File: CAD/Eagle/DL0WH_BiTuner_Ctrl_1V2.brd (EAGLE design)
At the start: 96.5 x 73 mm, 157 parts, among them Q0321 ABS07-32.768KHZ, U0101 STM32L476RXT_64PIN_LDO, U0601 MC33996, U0701 MC33996, U0801 MC33996, U0921 TS5A23166, U0941 LM2611, U0951 OPA354, U0961 OPA354, U0962 MCP4661-103E-MS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

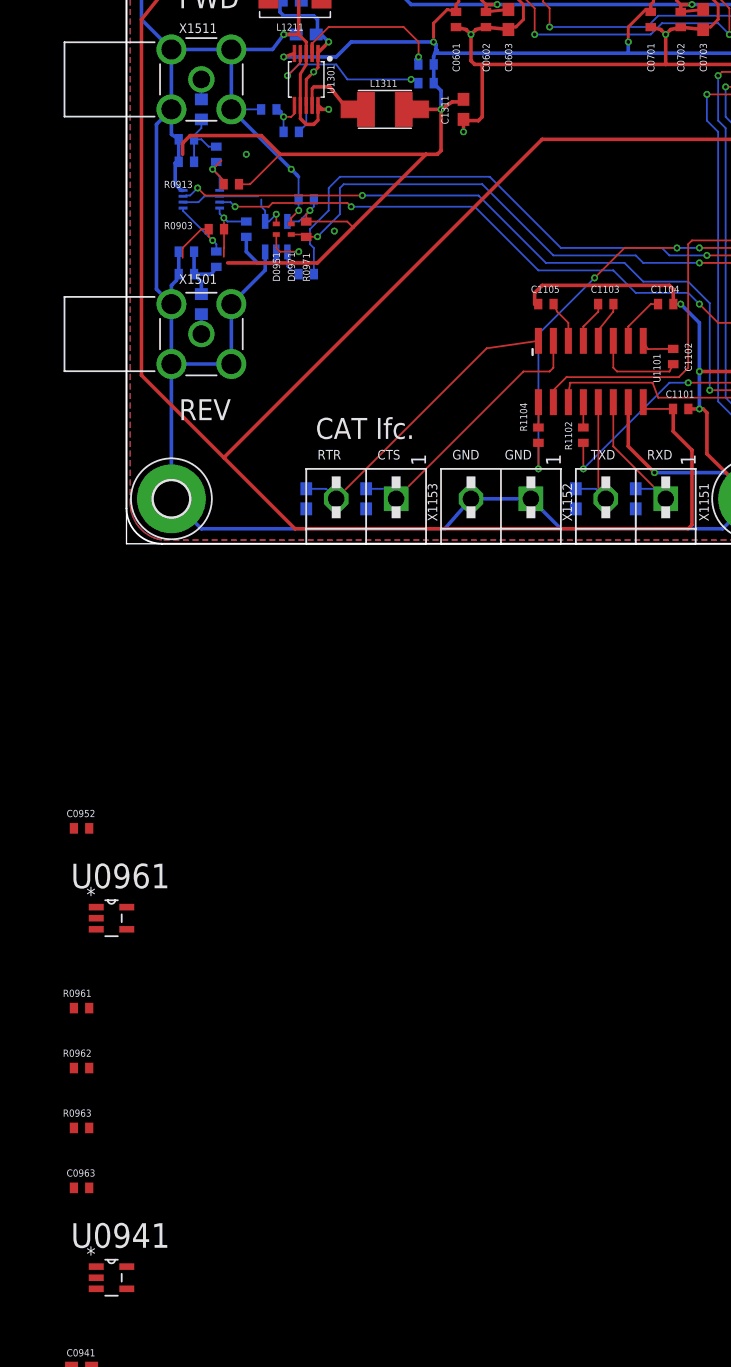
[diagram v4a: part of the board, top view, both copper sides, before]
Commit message: HW_1V2 - CAD/Eagle/lbr - df4iah_opamp package SOT-23-5 and SOT-23-6 text size fixed
Signed-off-by: Ulrich Habel <espero7757@gmx.net>
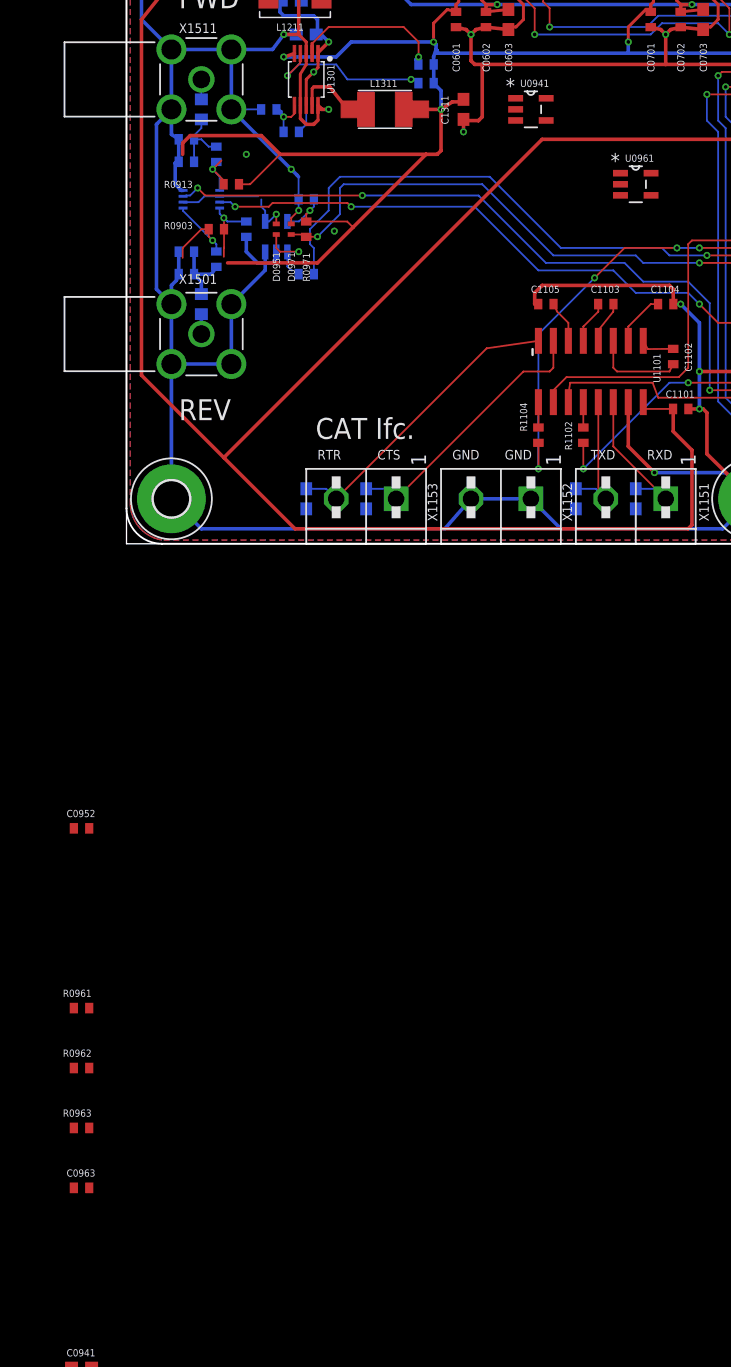
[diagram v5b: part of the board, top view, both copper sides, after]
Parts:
- moved U0941 105.2 mm to (34.3, 36.8)
- moved U0961 76.5 mm to (43.2, 30.5)
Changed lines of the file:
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@@
 <element name="D1221" library="df4iah_diode" package="SOD80C" value="CRS08" x="83.82" y="29.21" rot="R270"/>
 <element name="C0952" library="df4iah_rcl" package="C0402" value="100nF" x="-3.81" y="-24.13"/>
-<element name="U0961" library="df4iah_opamp" package="SOT-23-5" value="OPA354" x="-1.27" y="-31.75">
-<attribute name="OC_NEWARK" value="-" x="-1.27" y="-31.75" size="0.6096" layer="27" ratio="10" display="off"/>
-<attribute name="SUPPLIER" value="Texas Instruments" x="-1.27" y="-31.75" size="0.6096" layer="27" ratio="10" display="off"/>
-<attribute name="PACKAGE" value="SOT-23-5" x="-1.27" y="-31.75" size="0.6096" layer="27" ratio="10" display="off"/>
-<attribute name="MPN" value="OPA354AIDBVT" x="-1.27" y="-31.75" size="0.6096" layer="27" ratio="10" display="off"/>
-<attribute name="OC_FARNELL" value="1207050" x="-1.27" y="-31.75" size="0.6096" layer="27" ratio="10" display="off"/>
+<element name="U0961" library="df4iah_opamp" package="SOT-23-5" value="OPA354" x="43.18" y="30.48">
+<attribute name="OC_NEWARK" value="-" x="43.18" y="30.48" size="0.6096" layer="27" ratio="10" display="off"/>
+<attribute name="SUPPLIER" value="Texas Instruments" x="43.18" y="30.48" size="0.6096" layer="27" ratio="10" display="off"/>
+<attribute name="PACKAGE" value="SOT-23-5" x="43.18" y="30.48" size="0.6096" layer="27" ratio="10" display="off"/>
+<attribute name="MPN" value="OPA354AIDBVT" x="43.18" y="30.48" size="0.6096" layer="27" ratio="10" display="off"/>
+<attribute name="OC_FARNELL" value="1207050" x="43.18" y="30.48" size="0.6096" layer="27" ratio="10" display="off"/>
 </element>
 <element name="R0961" library="df4iah_rcl" package="R0402" value="1kR" x="-3.81" y="-39.37"/>
@@
 <element name="R0963" library="df4iah_rcl" package="R0402" value="10kR" x="-3.81" y="-49.53"/>
 <element name="C0963" library="df4iah_rcl" package="C0402" value="100pF" x="-3.81" y="-54.61"/>
-<element name="U0941" library="df4iah_powersupply" package="SOT95P280X145-5N" value="LM2611" x="-1.27" y="-62.23"/>
+<element name="U0941" library="df4iah_powersupply" package="SOT95P280X145-5N" value="LM2611" x="34.29" y="36.83"/>
 <element name="C0941" library="df4iah_rcl" package="C0603" value="22uF" x="-3.81" y="-69.85"/>
 <element name="L0941" library="df4iah_rcl" package="L1812" value="20uH" x="-2.54" y="-76.2"/>
@@
 <wire x1="-9.32" y1="-90.17" x2="-8.04" y2="-95.25" width="0" layer="19" extent="1-1"/>
 <wire x1="-2.96" y1="-69.85" x2="-9.32" y2="-90.17" width="0" layer="19" extent="1-1"/>
-<wire x1="-2.5654" y1="-62.23" x2="-2.96" y2="-69.85" width="0" layer="19" extent="1-1"/>
-<wire x1="-2.5654" y1="-32.6898" x2="-2.5654" y2="-62.23" width="0" layer="19" extent="1-1"/>
-<wire x1="-3.16" y1="-24.13" x2="-2.5654" y2="-32.6898" width="0" layer="19" extent="1-1"/>
+<wire x1="32.9946" y1="36.83" x2="-2.96" y2="-69.85" width="0" layer="19" extent="1-1"/>
+<wire x1="41.8846" y1="29.5402" x2="32.9946" y2="36.83" width="0" layer="19" extent="1-1"/>
+<wire x1="-3.16" y1="-24.13" x2="41.8846" y2="29.5402" width="0" layer="19" extent="1-1"/>
 <wire x1="6.35" y1="1.27" x2="-3.16" y2="-24.13" width="0" layer="19" extent="1-16"/>
 <wire x1="15.3875" y1="53.295" x2="14.2875" y2="53.295" width="0" layer="19" extent="1-1"/>
@@
 <wire x1="-0.59" y1="-76.2" x2="-4.375" y2="-116.78" width="0" layer="19" extent="1-1"/>
 <wire x1="-4.66" y1="-69.85" x2="-0.59" y2="-76.2" width="0" layer="19" extent="1-1"/>
-<wire x1="0.0254" y1="-63.1698" x2="-4.66" y2="-69.85" width="0" layer="19" extent="1-1"/>
-<wire x1="0.0254" y1="-61.2902" x2="0.0254" y2="-63.1698" width="0" layer="19" extent="1-1"/>
-<wire x1="0.0254" y1="-30.8102" x2="0.0254" y2="-61.2902" width="0" layer="19" extent="1-1"/>
-<wire x1="8.5725" y1="23.8125" x2="0.0254" y2="-30.8102" width="0" layer="19" extent="1-1"/>
+<wire x1="35.5854" y1="35.8902" x2="-4.66" y2="-69.85" width="0" layer="19" extent="1-1"/>
+<wire x1="35.5854" y1="37.7698" x2="35.5854" y2="35.8902" width="0" layer="19" extent="1-1"/>
+<wire x1="44.4754" y1="31.4198" x2="35.5854" y2="37.7698" width="0" layer="19" extent="1-1"/>
+<wire x1="8.5725" y1="23.8125" x2="44.4754" y2="31.4198" width="0" layer="19" extent="1-1"/>
 <wire x1="8.255" y1="24.335" x2="8.5725" y2="23.8125" width="0" layer="19" extent="1-1"/>
 </signal>
@@
 <wire x1="-9.74" y1="-95.25" x2="-6.97" y2="-100.33" width="0" layer="19" extent="1-1"/>
 <wire x1="-9.57" y1="-83.82" x2="-9.74" y2="-95.25" width="0" layer="19" extent="1-1"/>
-<wire x1="-2.5654" y1="-31.75" x2="-9.57" y2="-83.82" width="0" layer="19" extent="1-1"/>
-<wire x1="-4.46" y1="-24.13" x2="-2.5654" y2="-31.75" width="0" layer="19" extent="1-1"/>
+<wire x1="41.8846" y1="30.48" x2="-9.57" y2="-83.82" width="0" layer="19" extent="1-1"/>
+<wire x1="-4.46" y1="-24.13" x2="41.8846" y2="30.48" width="0" layer="19" extent="1-1"/>
 <wire x1="12.7" y1="24.7396" x2="-4.46" y2="-24.13" width="0" layer="19" extent="1-16"/>
 </signal>
@@
 <wire x1="-4.46" y1="-44.45" x2="-4.46" y2="-54.61" width="0" layer="19" extent="1-1"/>
 <wire x1="-3.16" y1="-39.37" x2="-4.46" y2="-44.45" width="0" layer="19" extent="1-1"/>
-<wire x1="0.0254" y1="-32.6898" x2="-3.16" y2="-39.37" width="0" layer="19" extent="1-1"/>
+<wire x1="44.4754" y1="29.5402" x2="-3.16" y2="-39.37" width="0" layer="19" extent="1-1"/>
 </signal>
 <signal name="SWR_OP2_OUT">
@@
 <contactref element="C0963" pad="2"/>
 <wire x1="-3.16" y1="-49.53" x2="-3.16" y2="-54.61" width="0" layer="19" extent="1-1"/>
-<wire x1="-2.5654" y1="-30.8102" x2="-3.16" y2="-49.53" width="0" layer="19" extent="1-1"/>
-<wire x1="14.59" y1="22.86" x2="-2.5654" y2="-30.8102" width="0" layer="19" extent="1-16"/>
+<wire x1="41.8846" y1="31.4198" x2="-3.16" y2="-49.53" width="0" layer="19" extent="1-1"/>
+<wire x1="14.59" y1="22.86" x2="41.8846" y2="31.4198" width="0" layer="19" extent="1-16"/>
 </signal>
 <signal name="LM2611_SW">
@@
 <contactref element="C0942" pad="1"/>
 <wire x1="-4.49" y1="-76.2" x2="-9.84" y2="-77.47" width="0" layer="19" extent="1-1"/>
-<wire x1="-2.5654" y1="-61.2902" x2="-4.49" y2="-76.2" width="0" layer="19" extent="1-1"/>
+<wire x1="32.9946" y1="37.7698" x2="-4.49" y2="-76.2" width="0" layer="19" extent="1-1"/>
 </signal>
 <signal name="LM_DA">
@@
 <wire x1="-6.97" y1="-105.41" x2="-9.54" y2="-110.49" width="0" layer="19" extent="1-1"/>
 <wire x1="-8.27" y1="-100.33" x2="-6.97" y2="-105.41" width="0" layer="19" extent="1-1"/>
-<wire x1="-2.5654" y1="-63.1698" x2="-8.27" y2="-100.33" width="0" layer="19" extent="1-1"/>
+<wire x1="32.9946" y1="35.8902" x2="-8.27" y2="-100.33" width="0" layer="19" extent="1-1"/>
 </signal>
 <signal name="OPA_PULL">

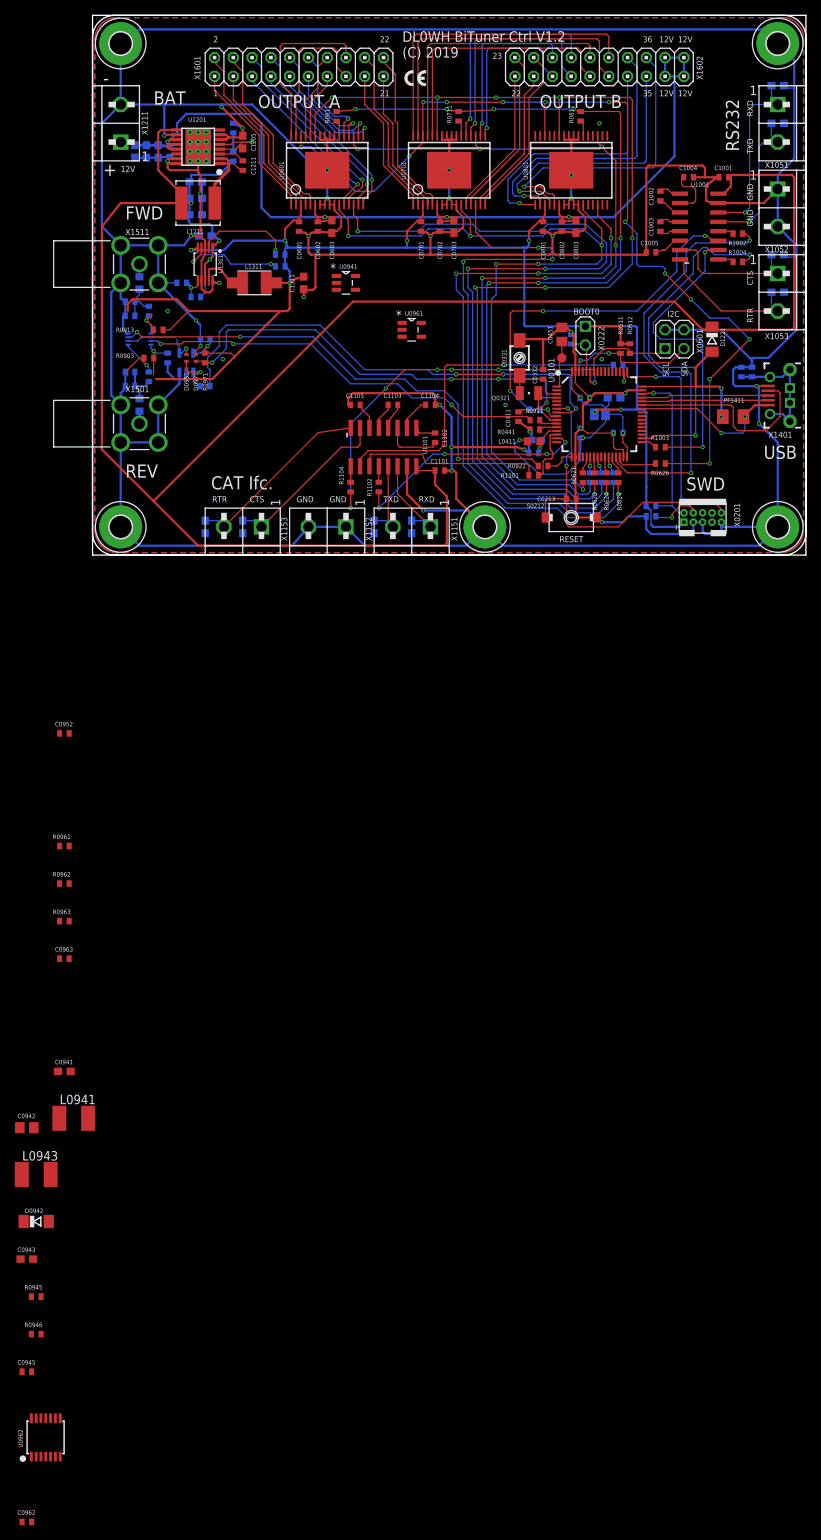
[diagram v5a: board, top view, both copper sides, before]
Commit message: HW_1V2 - CAD/Eagle - new LogAmp module placed
Signed-off-by: Ulrich Habel <espero7757@gmx.net>
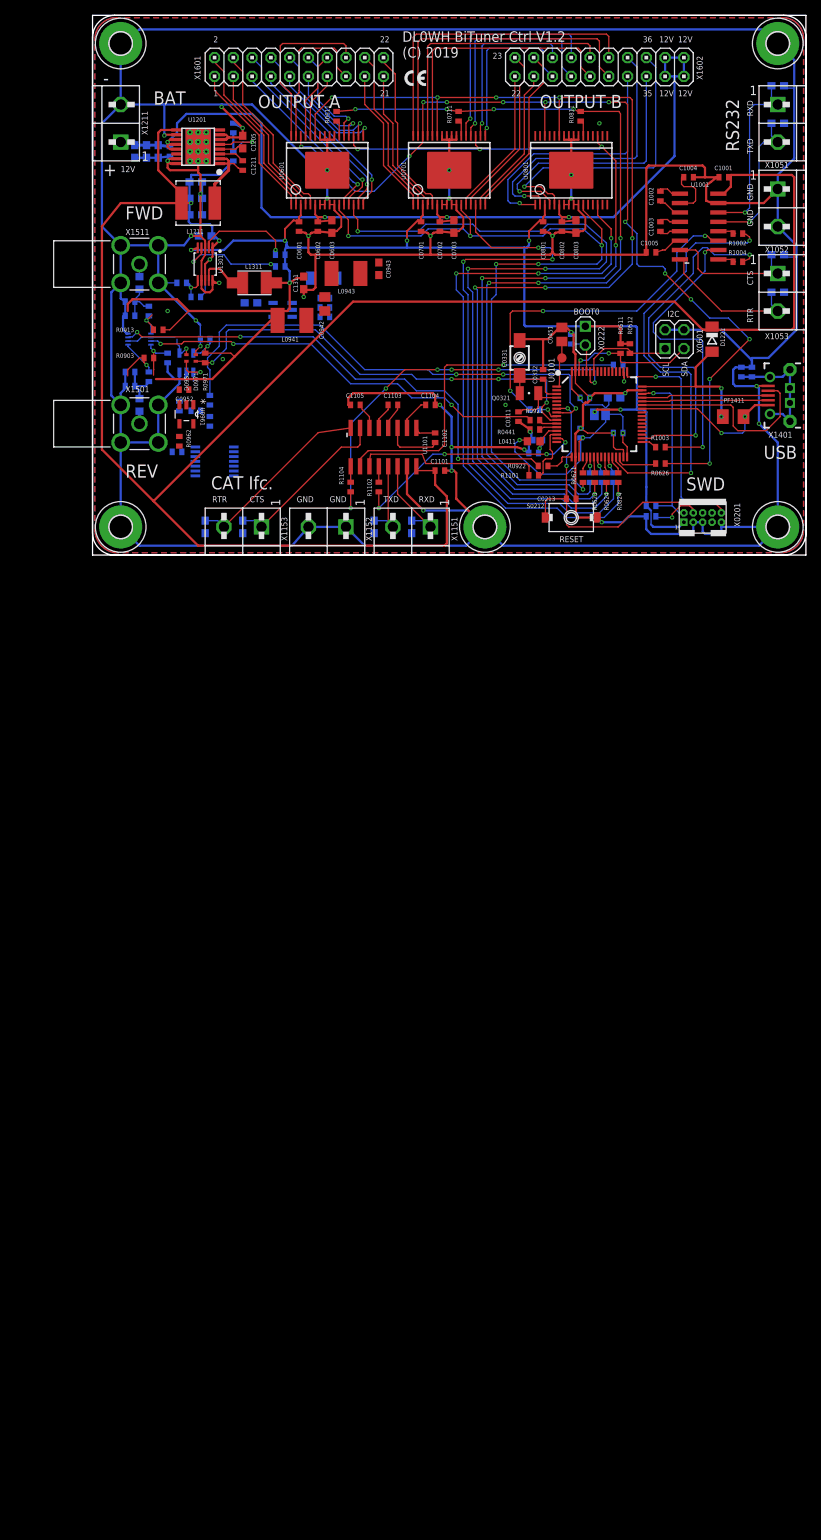
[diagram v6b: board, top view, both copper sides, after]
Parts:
- moved C0945 149.5 mm to (31.4, 33.5), flipped to the bottom, turned to 180 degrees
- moved C0962 146.2 mm to (11.4, 14.0), flipped to the bottom
- moved R0946 145.5 mm to (31.4, 34.8), flipped to the bottom
- moved C0943 142.2 mm to (38.7, 38.7), turned to 90 degrees
- moved R0945 138.2 mm to (31.4, 32.2), flipped to the bottom, turned to 180 degrees
- moved U0962 134.0 mm to (16.5, 12.7), flipped to the bottom, turned to 270 degrees
- moved D0942 133.4 mm to (31.3, 37.5), flipped to the bottom, turned to 180 degrees
- moved L0943 128.9 mm to (34.3, 38.1), turned to 180 degrees
- moved C0942 118.5 mm to (31.4, 34.0), turned to 90 degrees
- moved L0941 111.9 mm to (27.0, 31.8), turned to 180 degrees
- moved C0941 107.0 mm to (21.4, 34.1), flipped to the bottom
- moved C0963 76.2 mm to (14.0, 19.5), flipped to the bottom, turned to 180 degrees
- moved R0963 70.4 mm to (15.9, 18.1), flipped to the bottom, turned to 90 degrees
- moved R0962 61.8 mm to (11.7, 15.4), turned to 270 degrees
- moved R0961 61.5 mm to (11.7, 20.2), flipped to the bottom, turned to 270 degrees
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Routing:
- net PC0: track 66.4 -> 67.7 mm
- net SWR_OP1_OUT: track 5.95 -> 5.38 mm

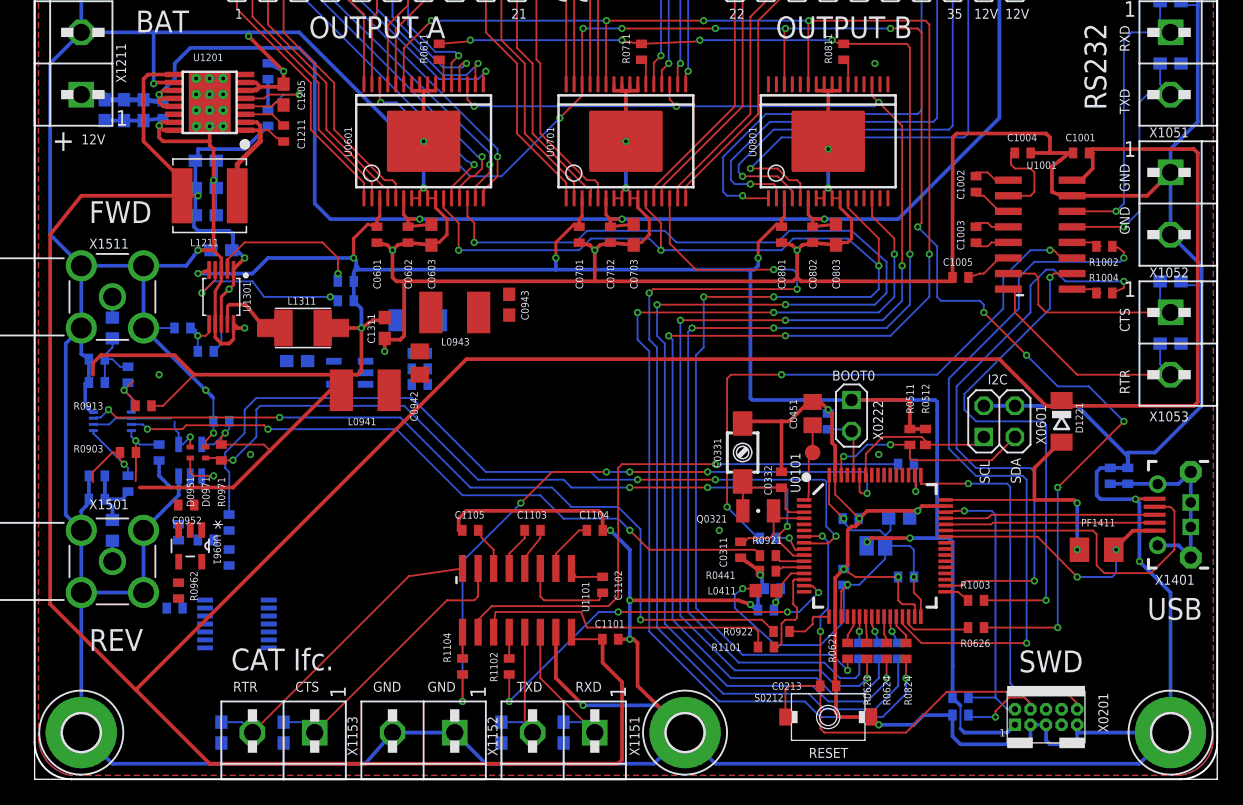
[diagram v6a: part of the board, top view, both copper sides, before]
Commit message: HW_1V2 - CAD/Eagle/lbr - df4iah_connector SWD-connector restring change
Signed-off-by: Ulrich Habel <espero7757@gmx.net>
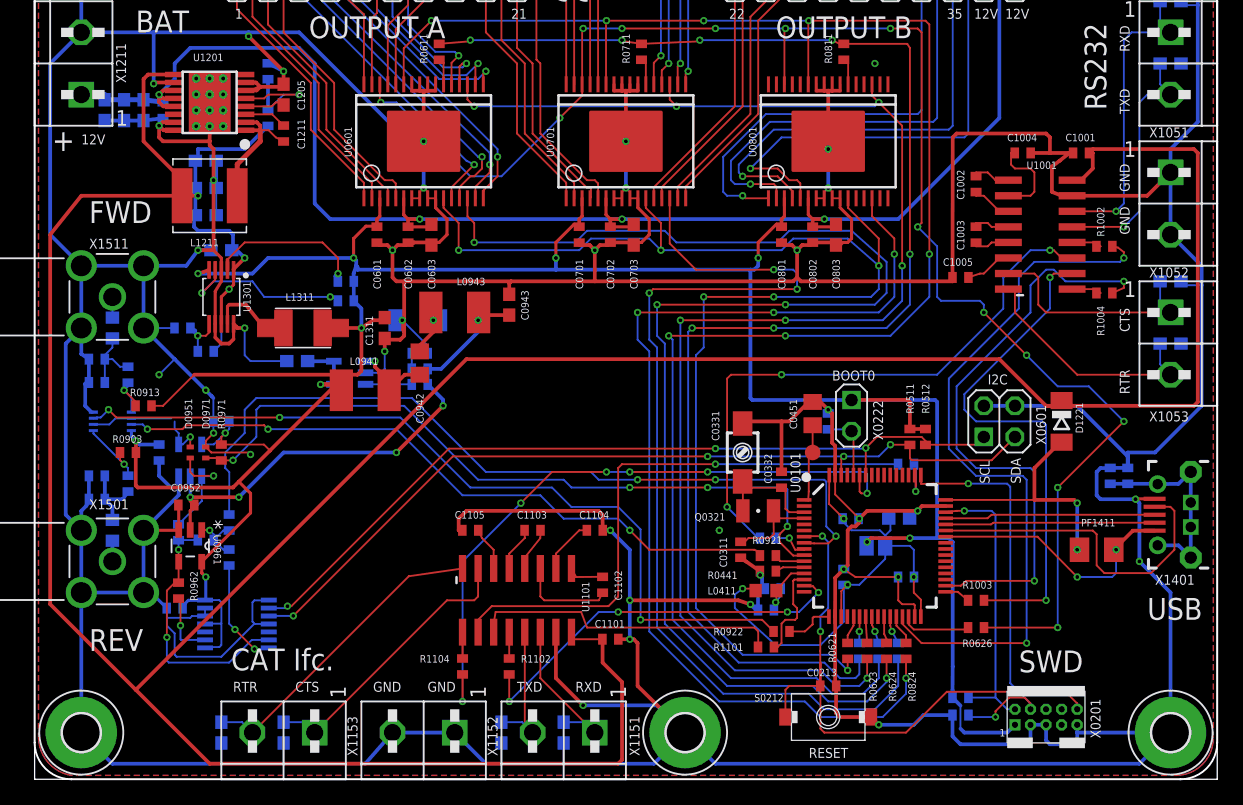
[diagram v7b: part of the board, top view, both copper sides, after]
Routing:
- net PB6: track 12.7 -> 67.2 mm, vias 0 -> 3
- net PB9: track 17.9 -> 70.3 mm, vias 2 -> 4
- net GND: track 854.6 -> 902.4 mm
- net -1V5: track 0.00 -> 41.5 mm, vias 0 -> 5
- net SWR_OP2_IN: track 0.00 -> 21.1 mm, vias 0 -> 2
- net +3V3: track 220.2 -> 240.7 mm, vias 9 -> 11
- net OPA_FB: track 0.00 -> 9.04 mm, vias 0 -> 2
- net LM2611_SW: track 0.00 -> 6.48 mm, vias 0 -> 1
- net LM2611_NFB: track 0.00 -> 6.31 mm
- net OPA_PULL: track 0.00 -> 5.43 mm, vias 0 -> 1
- net SWR_OP2_OUT: track 0.00 -> 4.74 mm, vias 0 -> 1
- net LM_DA: track 0.00 -> 4.71 mm, vias 0 -> 1
- net SWR_IN_FWD: track 9.64 -> 5.94 mm
- net SWR_OP1_OUT: track 5.38 -> 8.86 mm
- net SWR_IN_REV: track 5.50 -> 4.45 mm
